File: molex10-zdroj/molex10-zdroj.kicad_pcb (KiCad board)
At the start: 2 copper layers, 52 x 52 mm, 9 parts, among them J1 MVE253-5-V, J2 TME 39281103 MOLEX, J3 MVE253-5-V, J4 MVE252-5-V, J5 MVE252-5-V

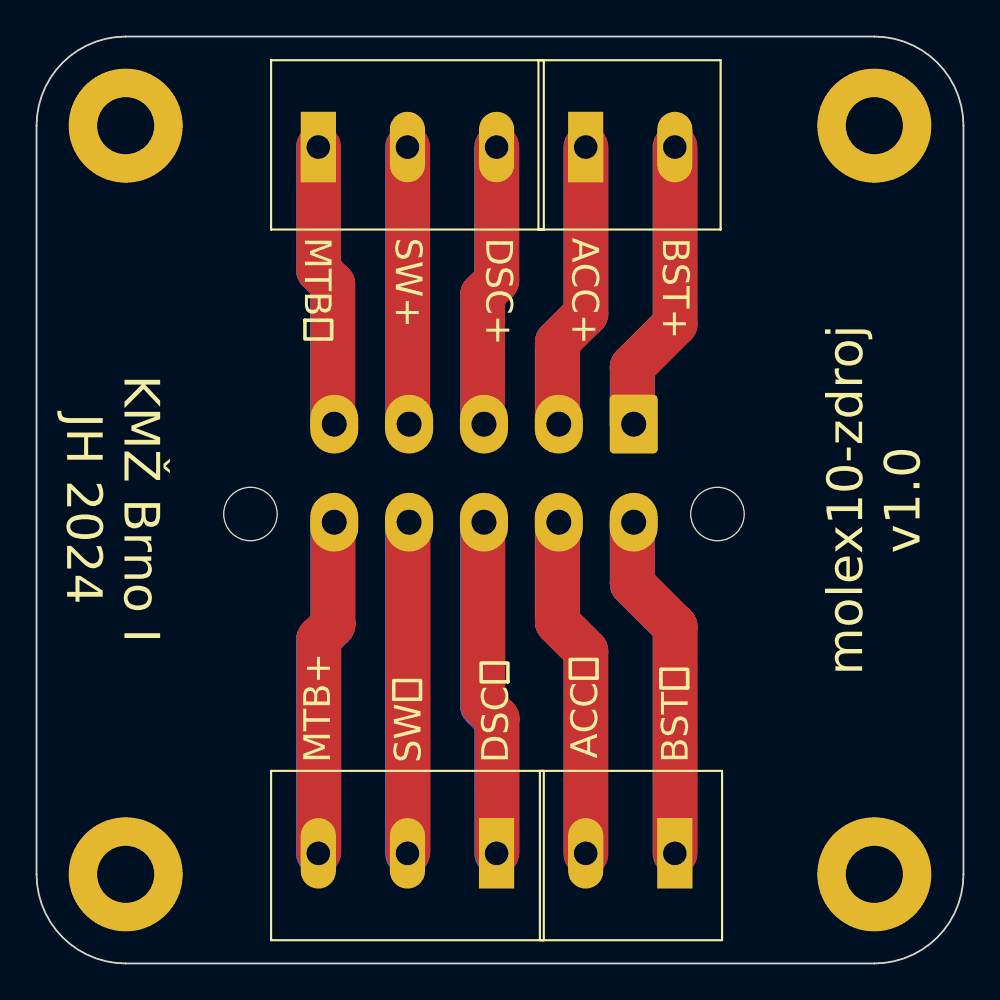
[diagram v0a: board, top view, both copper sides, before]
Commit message: molex10-zdroj: center MOLEX connector horizontally.
PCB v1.1
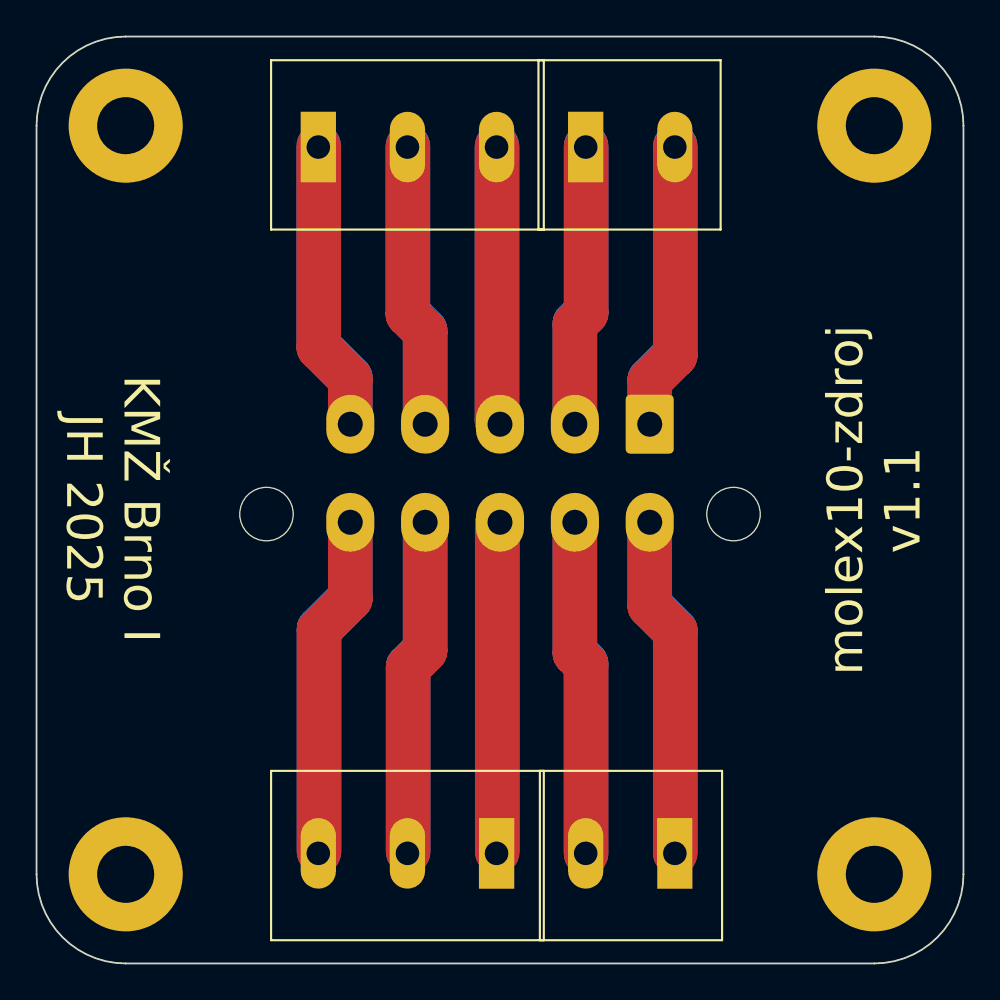
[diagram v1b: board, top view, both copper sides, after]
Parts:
- moved J2 0.90 mm to (114.9, 91.8)
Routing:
- net /MTB: track 39.1 -> 38.3 mm
- net /SWITCH: track 31.1 -> 31.9 mm
- net /BOOST+: track 31.8 -> 32.6 mm
- net /GND: track 33.1 -> 32.3 mm
- net /ACC: track 32.4 -> 31.6 mm
- net /GND-ACC: track 38.5 -> 37.7 mm
- net /GND-DSC: track 37.8 -> 37.1 mm
- net /GND-SWITCH: track 37.2 -> 37.8 mm
- net /BOOST-: track 37.8 -> 38.5 mm
- net /DSC: track 31.8 -> 31.2 mm
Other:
- board text added: "KMŽ Brno I JH 2025"
- board text added: "molex10-zdroj v1.1"
- board text removed: "ACC+"
- board text removed: "ACC⏚"
- board text removed: "BST+"
- board text removed: "BST⏚"
- board text removed: "DSC+"
- board text removed: "DSC⏚"
- board text removed: "KMŽ Brno I JH 2024"
- board text removed: "MTB+"
- board text removed: "MTB⏚"
- board text removed: "SW+"
- board text removed: "SW⏚"
- board text removed: "molex10-zdroj v1.0"

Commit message: molex10-zdroj: update to KiCad 9, add silkscreen desc.
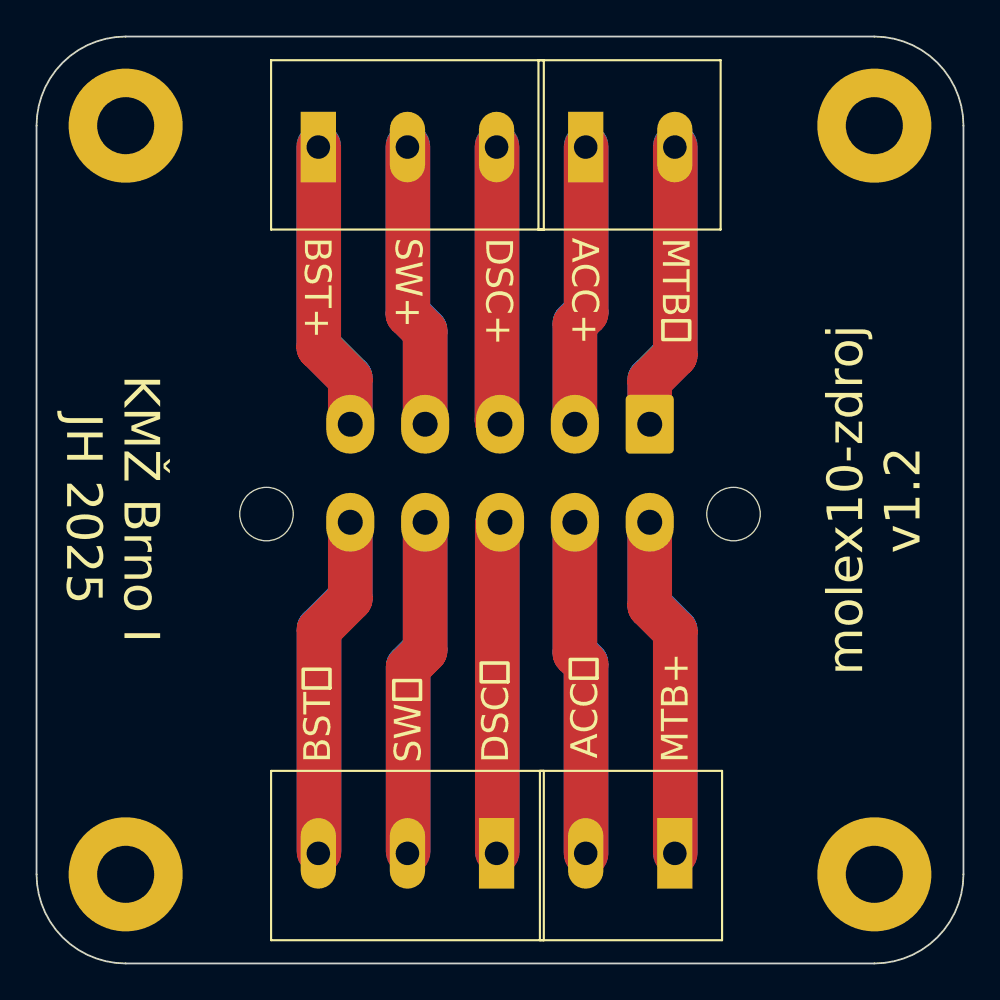
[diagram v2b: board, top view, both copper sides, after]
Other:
- board text added: "ACC+"
- board text added: "ACC⏚"
- board text added: "BST+"
- board text added: "BST⏚"
- board text added: "DSC+"
- board text added: "DSC⏚"
- board text added: "MTB+"
- board text added: "MTB⏚"
- board text added: "SW+"
- board text added: "SW⏚"
- board text added: "molex10-zdroj v1.2"
- board text removed: "molex10-zdroj v1.1"
